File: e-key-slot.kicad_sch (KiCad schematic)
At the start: 0 parts

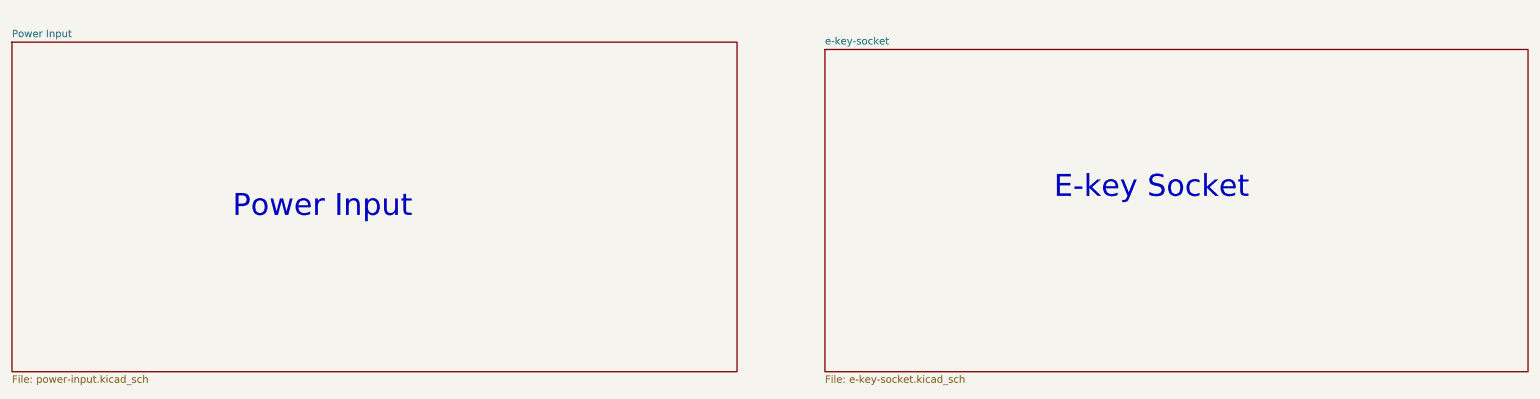
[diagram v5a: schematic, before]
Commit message: Replace dual holder with single holder
Signed-off-by: JeffMboya <jangina.mboya@gmail.com>
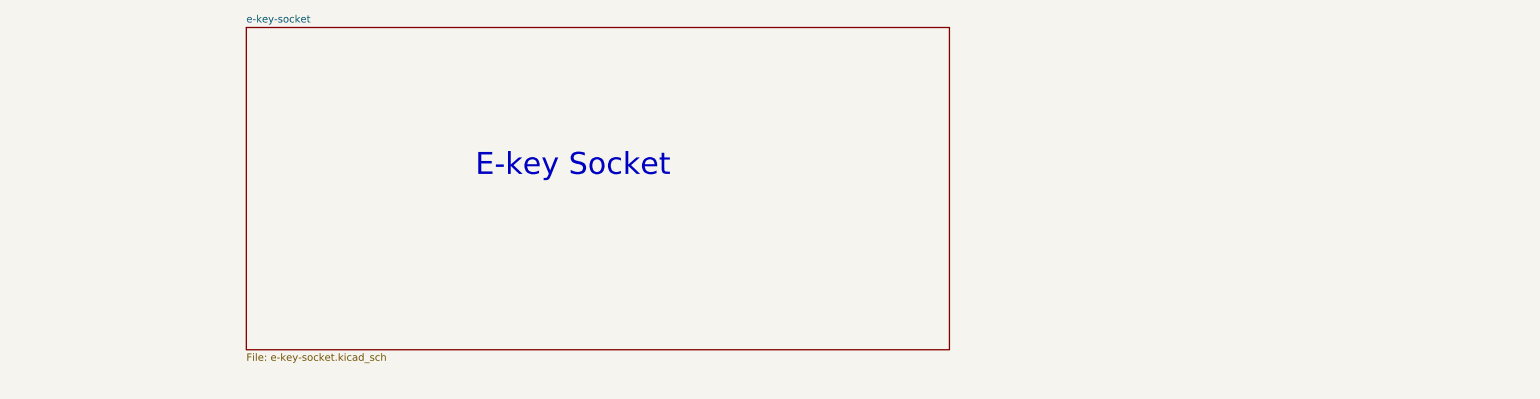
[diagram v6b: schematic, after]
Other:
- removed sheet Power Input
- note removed: "Power Input"
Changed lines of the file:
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@@
 	(text "E-key Socket"
 		(exclude_from_sim no)
-		(at 215.392 49.276 0)
+		(at 115.062 45.466 0)
 		(effects
 			(font
@@
 		)
 	)
-	(text "Power Input"
-		(exclude_from_sim no)
-		(at 71.628 52.578 0)
-		(effects
-			(font
-				(size 3.81 3.81)
-				(color 0 0 0 1)
-			)
-		)
-	)
 	(sheet
-		(at 158.75 25.4)
+		(at 58.42 21.59)
 		(size 121.92 55.88)
 		(fields_autoplaced yes)
@@
 		)
 		(property "Sheetname" "e-key-socket"
-			(at 158.75 24.6884 0)
+			(at 58.42 20.8784 0)
 			(effects
 				(font
@@
 		)
 		(property "Sheetfile" "e-key-socket.kicad_sch"
-			(at 158.75 81.8646 0)
+			(at 58.42 78.0546 0)
 			(effects
 				(font
@@
 			)
 		)
-		(instances
-			(project "e-key-slot"
-				(path "/c124244a-3c1c-475d-932f-950445d8391e"
-					(page "4")
-				)
-			)
-		)
-	)
-	(sheet
-		(at 17.78 24.13)
-		(size 125.73 57.15)
-		(fields_autoplaced yes)
-		(stroke
-			(width 0.1524)
-			(type solid)
-		)
-		(fill
-			(color 150 55 37 1.0000)
-		)
-		(property "Sheetname" "Power Input"
-			(at 17.78 23.4184 0)
-			(effects
-				(font
-					(size 1.27 1.27)
-				)
-				(justify left bottom)
-			)
-		)
-		(property "Sheetfile" "power-input.kicad_sch"
-			(at 17.78 81.8646 0)
-			(effects
-				(font
-					(size 1.27 1.27)
-				)
-				(justify left top)
-			)
-		)
-		(property "Field2" ""
-			(at 17.78 24.13 0)
-			(effects
-				(font
-					(size 1.27 1.27)
-				)
-				(hide yes)
-			)
-		)
